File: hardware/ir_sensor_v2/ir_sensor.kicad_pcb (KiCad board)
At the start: 2 copper layers, 45.5 x 71 mm, 32 parts, among them J1 Conn_01x04, J10 Conn_01x02, J11 Conn_01x02, J12 Conn_01x02, J13 Conn_01x02, J2 Conn_01x04, J3 Conn_01x04, J4 Conn_01x02, J5 Conn_01x02, J6 Conn_01x02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

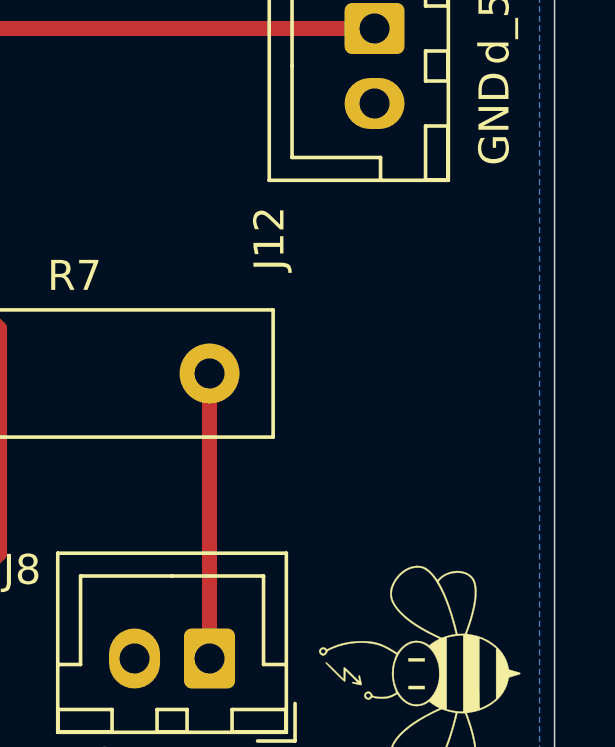
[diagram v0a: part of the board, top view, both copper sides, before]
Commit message: Add board name and version on silkscreen
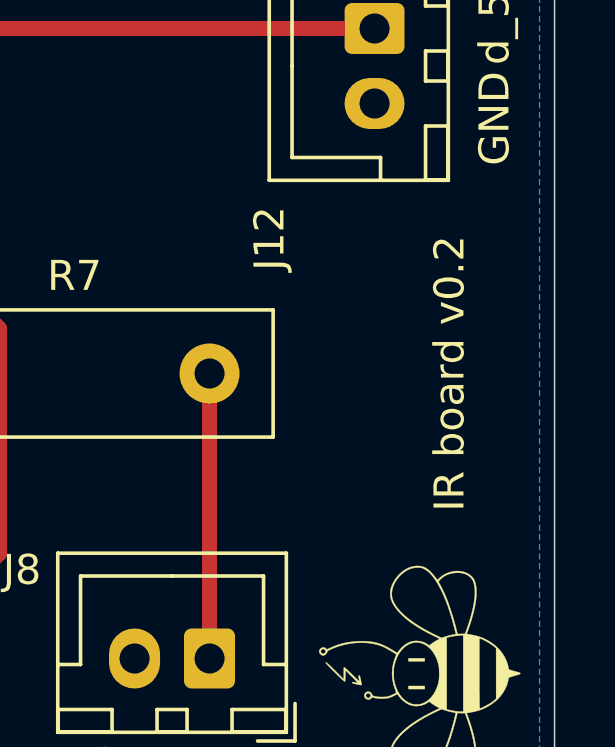
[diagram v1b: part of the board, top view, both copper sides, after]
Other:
- board text added: "IR board v0.2"

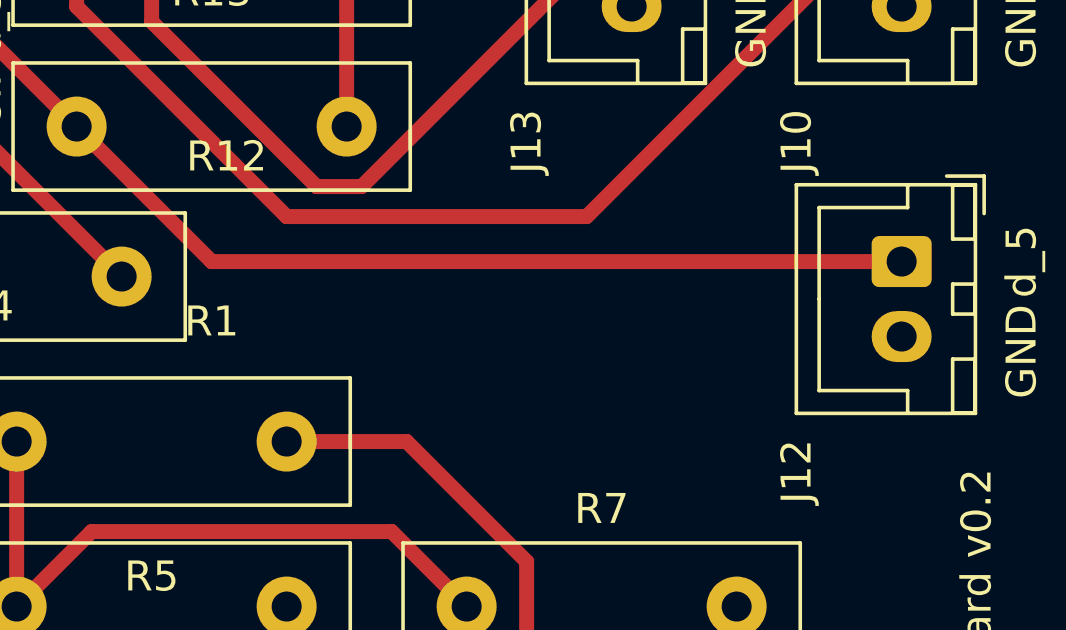
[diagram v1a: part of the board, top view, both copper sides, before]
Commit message: Apply CERN-W license
Apply CERN-W license to all boards, move the first iteration of the IR_sensor to the archive

Co-Authored-By: Andre Maia Chagas <a.maia-chagas@sussex.ac.uk>
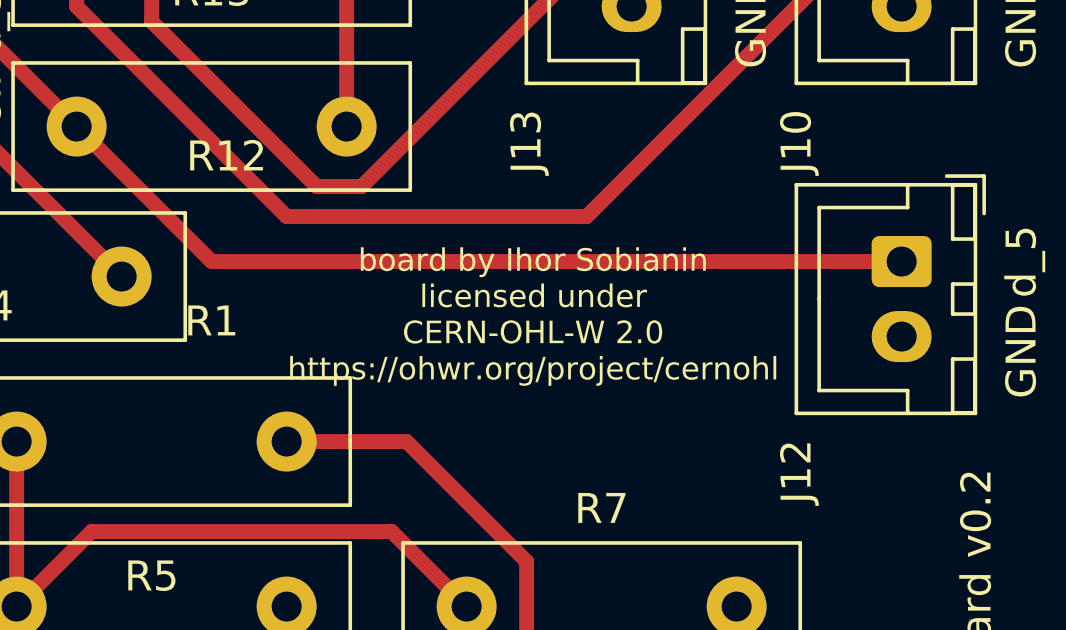
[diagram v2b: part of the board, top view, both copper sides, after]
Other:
- board text added: "board by Ihor Sobianin licensed under CERN-OHL-W 2.0 https://ohwr.org/project/cernohl"
